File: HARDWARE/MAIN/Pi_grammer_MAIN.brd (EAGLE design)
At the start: 73.7 x 78.7 mm, 51 parts, among them J1 TARGET_copy, Q1 BSS138, Q2 BSS138, Q3 BSS138, Q4 BSS138, U1 AT42QT1010UDFN

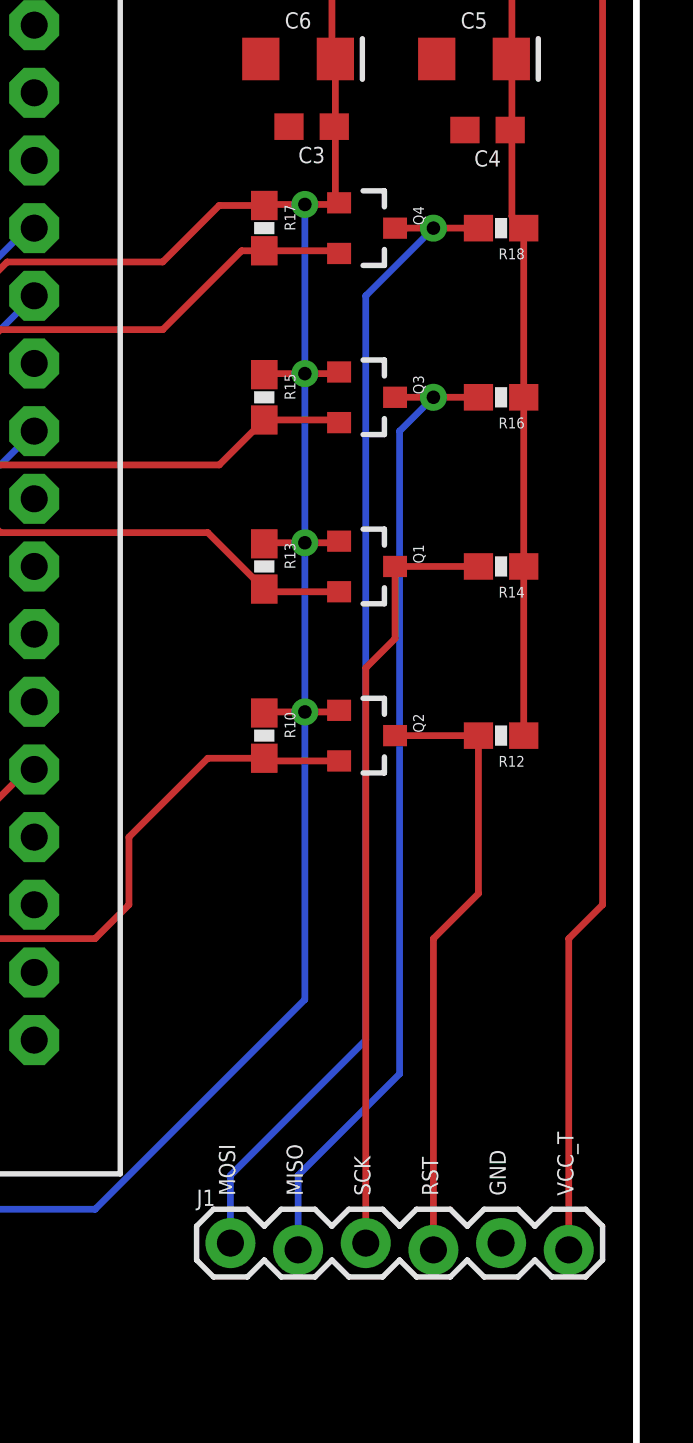
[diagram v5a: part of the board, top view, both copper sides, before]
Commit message: BOM update - library and PROD_ID stuff
No change to design, just did a replace to correct parts in library.

Note, I also had to manually adjust the PROD_ID for the RA header,
because I didn't want to muddy up the device for this part.
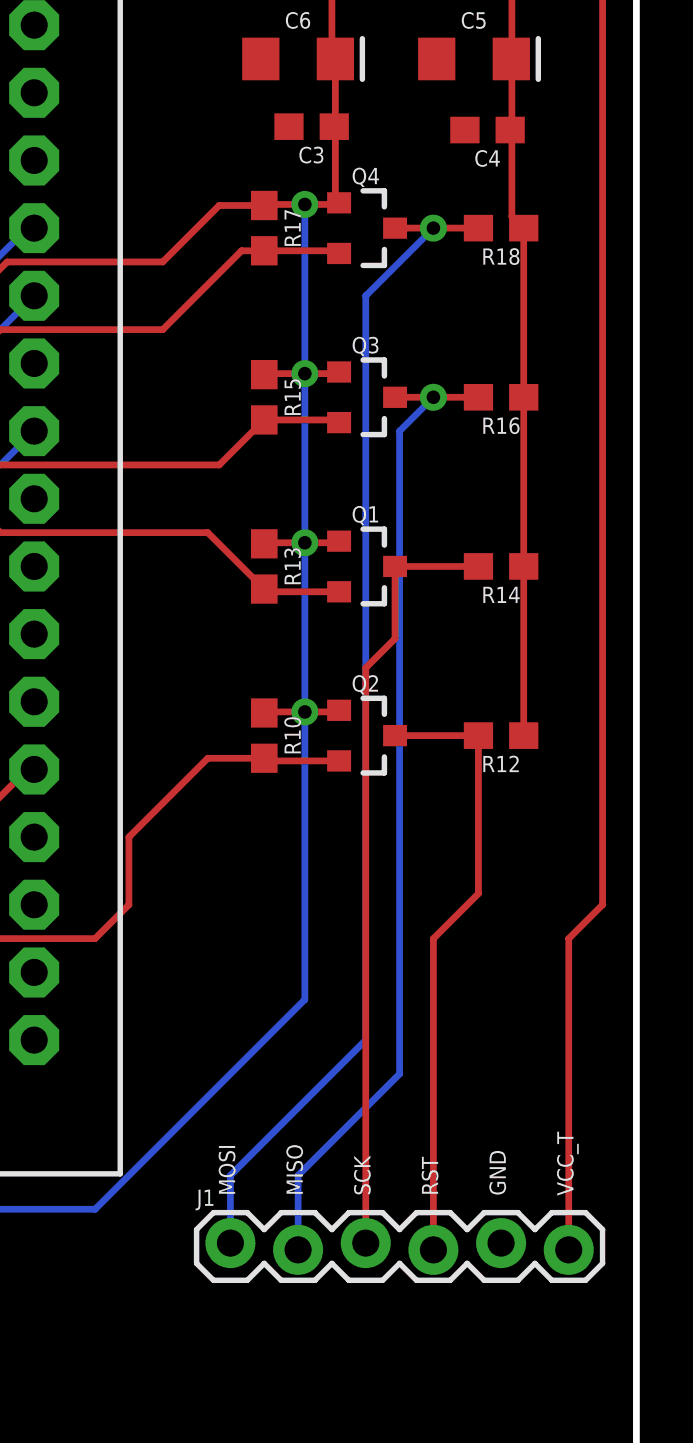
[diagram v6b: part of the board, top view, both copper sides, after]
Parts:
- J1: device SparkFun-Connectors:1X06-SIP_LOCK -> SparkFun-Connectors:1X06_LOCK
- Q1, Q2, Q3, Q4: value BSS138 -> 220mA/50V/3.5Ω; device SparkFun:SOT23-3 -> SparkFun-DiscreteSemi:SOT23-3
- R10, R12, R13, R14, R15, R16, R17, R18: value 10K -> 10k; device SparkFun:0603-RES -> SparkFun-Resistors:0603
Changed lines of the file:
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@@
 <element name="FD1" library="SparkFun-Aesthetics" package="MICRO-FIDUCIAL" value="FIDUCIALUFIDUCIAL" x="2.54" y="76.2"/>
 <element name="FD2" library="SparkFun-Aesthetics" package="MICRO-FIDUCIAL" value="FIDUCIALUFIDUCIAL" x="72.39" y="2.54"/>
-<element name="Q2" library="SparkFun" package="SOT23-3" value="BSS138" x="63.5" y="33.02" rot="R270"/>
-<element name="R10" library="SparkFun" package="0603-RES" value="10K" x="59.69" y="33.02" rot="R270"/>
-<element name="R12" library="SparkFun" package="0603-RES" value="10K" x="68.58" y="33.02" rot="R180"/>
-<element name="Q1" library="SparkFun" package="SOT23-3" value="BSS138" x="63.5" y="39.37" rot="R270"/>
-<element name="R13" library="SparkFun" package="0603-RES" value="10K" x="59.69" y="39.37" rot="R270"/>
-<element name="R14" library="SparkFun" package="0603-RES" value="10K" x="68.58" y="39.37" rot="R180"/>
-<element name="Q3" library="SparkFun" package="SOT23-3" value="BSS138" x="63.5" y="45.72" rot="R270"/>
-<element name="R15" library="SparkFun" package="0603-RES" value="10K" x="59.69" y="45.72" rot="R270"/>
-<element name="R16" library="SparkFun" package="0603-RES" value="10K" x="68.58" y="45.72" rot="R180"/>
-<element name="Q4" library="SparkFun" package="SOT23-3" value="BSS138" x="63.5" y="52.07" rot="R270"/>
-<element name="R17" library="SparkFun" package="0603-RES" value="10K" x="59.69" y="52.07" rot="R270"/>
-<element name="R18" library="SparkFun" package="0603-RES" value="10K" x="68.58" y="52.07" rot="R180"/>
-<element name="J1" library="SparkFun-Connectors" package="1X06-SIP_LOCK" value="TARGET_copy" x="58.42" y="13.97">
-<attribute name="PROD_ID" value="CONN-09698" x="58.42" y="13.97" size="1.778" layer="27" font="vector" ratio="15" display="off"/>
+<element name="Q2" library="SparkFun-DiscreteSemi" package="SOT23-3" value="220mA/50V/3.5Ω" x="63.5" y="33.02" rot="R270">
+<attribute name="PROD_ID" value="TRANS-00830" x="63.5" y="33.02" size="1.778" layer="27" rot="R270" display="off"/>
+<attribute name="VALUE" value="220mA/50V/3.5Ω" x="63.5" y="33.02" size="1.778" layer="27" rot="R270" display="off"/>
+</element>
+<element name="R10" library="SparkFun-Resistors" package="0603" value="10k" x="59.69" y="33.02" rot="R270">
+<attribute name="PROD_ID" value="RES-00824" x="59.69" y="33.02" size="1.778" layer="27" rot="R270" display="off"/>
+<attribute name="VALUE" value="10k" x="59.69" y="33.02" size="1.778" layer="27" rot="R270" display="off"/>
+</element>
+<element name="R12" library="SparkFun-Resistors" package="0603" value="10k" x="68.58" y="33.02" rot="R180">
+<attribute name="PROD_ID" value="RES-00824" x="68.58" y="33.02" size="1.778" layer="27" rot="R180" display="off"/>
+<attribute name="VALUE" value="10k" x="68.58" y="33.02" size="1.778" layer="27" rot="R180" display="off"/>
+</element>
+<element name="Q1" library="SparkFun-DiscreteSemi" package="SOT23-3" value="220mA/50V/3.5Ω" x="63.5" y="39.37" rot="R270">
+<attribute name="PROD_ID" value="TRANS-00830" x="63.5" y="39.37" size="1.778" layer="27" rot="R270" display="off"/>
+<attribute name="VALUE" value="220mA/50V/3.5Ω" x="63.5" y="39.37" size="1.778" layer="27" rot="R270" display="off"/>
+</element>
+<element name="R13" library="SparkFun-Resistors" package="0603" value="10k" x="59.69" y="39.37" rot="R270">
+<attribute name="PROD_ID" value="RES-00824" x="59.69" y="39.37" size="1.778" layer="27" rot="R270" display="off"/>
+<attribute name="VALUE" value="10k" x="59.69" y="39.37" size="1.778" layer="27" rot="R270" display="off"/>
+</element>
+<element name="R14" library="SparkFun-Resistors" package="0603" value="10k" x="68.58" y="39.37" rot="R180">
+<attribute name="PROD_ID" value="RES-00824" x="68.58" y="39.37" size="1.778" layer="27" rot="R180" display="off"/>
+<attribute name="VALUE" value="10k" x="68.58" y="39.37" size="1.778" layer="27" rot="R180" display="off"/>
+</element>
+<element name="Q3" library="SparkFun-DiscreteSemi" package="SOT23-3" value="220mA/50V/3.5Ω" x="63.5" y="45.72" rot="R270">
+<attribute name="PROD_ID" value="TRANS-00830" x="63.5" y="45.72" size="1.778" layer="27" rot="R270" display="off"/>
+<attribute name="VALUE" value="220mA/50V/3.5Ω" x="63.5" y="45.72" size="1.778" layer="27" rot="R270" display="off"/>
+</element>
+<element name="R15" library="SparkFun-Resistors" package="0603" value="10k" x="59.69" y="45.72" rot="R270">
+<attribute name="PROD_ID" value="RES-00824" x="59.69" y="45.72" size="1.778" layer="27" rot="R270" display="off"/>
+<attribute name="VALUE" value="10k" x="59.69" y="45.72" size="1.778" layer="27" rot="R270" display="off"/>
+</element>
+<element name="R16" library="SparkFun-Resistors" package="0603" value="10k" x="68.58" y="45.72" rot="R180">
+<attribute name="PROD_ID" value="RES-00824" x="68.58" y="45.72" size="1.778" layer="27" rot="R180" display="off"/>
+<attribute name="VALUE" value="10k" x="68.58" y="45.72" size="1.778" layer="27" rot="R180" display="off"/>
+</element>
+<element name="Q4" library="SparkFun-DiscreteSemi" package="SOT23-3" value="220mA/50V/3.5Ω" x="63.5" y="52.07" rot="R270">
+<attribute name="PROD_ID" value="TRANS-00830" x="63.5" y="52.07" size="1.778" layer="27" rot="R270" display="off"/>
+<attribute name="VALUE" value="220mA/50V/3.5Ω" x="63.5" y="52.07" size="1.778" layer="27" rot="R270" display="off"/>
+</element>
+<element name="R17" library="SparkFun-Resistors" package="0603" value="10k" x="59.69" y="52.07" rot="R270">
+<attribute name="PROD_ID" value="RES-00824" x="59.69" y="52.07" size="1.778" layer="27" rot="R270" display="off"/>
+<attribute name="VALUE" value="10k" x="59.69" y="52.07" size="1.778" layer="27" rot="R270" display="off"/>
+</element>
+<element name="R18" library="SparkFun-Resistors" package="0603" value="10k" x="68.58" y="52.07" rot="R180">
+<attribute name="PROD_ID" value="RES-00824" x="68.58" y="52.07" size="1.778" layer="27" rot="R180" display="off"/>
+<attribute name="VALUE" value="10k" x="68.58" y="52.07" size="1.778" layer="27" rot="R180" display="off"/>
+</element>
+<element name="J1" library="SparkFun-Connectors" package="1X06_LOCK" value="TARGET_copy" x="58.42" y="13.97">
+<attribute name="PROD_ID" value="CONN-10140" x="58.42" y="13.97" size="1.778" layer="27" font="vector" ratio="15" display="off"/>
 </element>
 <element name="JP5" library="SparkFun-Jumpers" package="SMT-JUMPER_2_NO_SILK" value="" x="68.58" y="69.85" rot="R180"/>

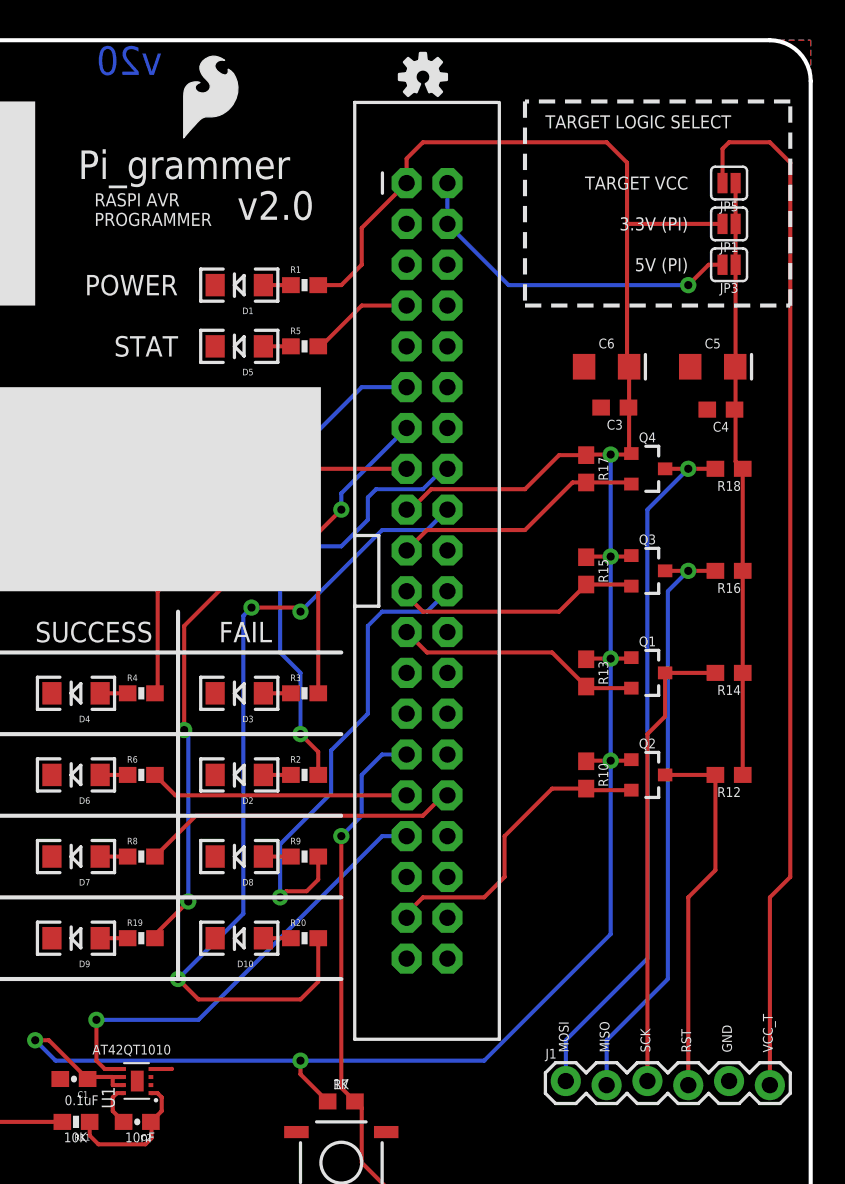
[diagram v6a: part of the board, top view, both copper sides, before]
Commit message: pi_grammer v21
Added in isolation switch
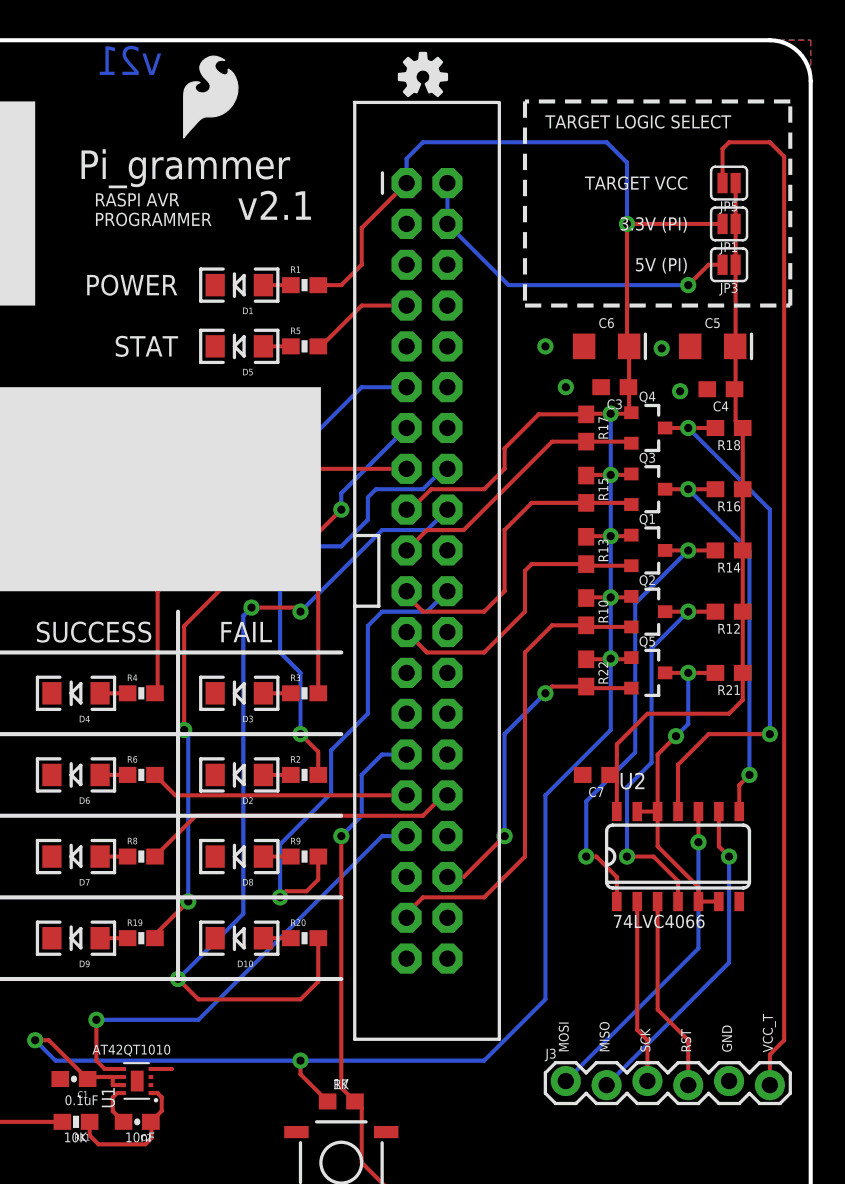
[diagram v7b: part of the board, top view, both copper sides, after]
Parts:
- added C7: 0.1uF, SparkFun-Capacitors:0603
- added Q5: 220mA/50V/3.5Ω, SparkFun-DiscreteSemi:SOT23-3
- added R21, R22: 10k, SparkFun-Resistors:0603
- added U2: 74LVC4066, Testing:SO14
- moved Q2 10.2 mm to (63.5, 43.2)
- moved R10 10.2 mm to (59.7, 43.2)
- moved R12 10.2 mm to (68.6, 43.2)
- moved Q1 7.62 mm to (63.5, 47.0)
- moved R13 7.62 mm to (59.7, 47.0)
- moved R14 7.62 mm to (68.6, 47.0)
- moved Q3 5.08 mm to (63.5, 50.8)
- moved R15 5.08 mm to (59.7, 50.8)
- moved R16 5.08 mm to (68.6, 50.8)
- moved Q4 2.54 mm to (63.5, 54.6)
- moved R17 2.54 mm to (59.7, 54.6)
- moved R18 2.54 mm to (68.6, 54.6)
- moved C4 1.27 mm to (68.1, 57.0)
- moved C3 1.27 mm to (61.5, 57.1)
- moved C5 1.27 mm to (67.6, 59.7)
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- renumbered J1 to J3
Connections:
- removed net N$9: C4.1, C5.+, JP1.1, JP3.1, JP5.1, R12.1, R14.1, R16.1, R18.1
- new net BRD_MISO: J3.2, U2.9
- new net BRD_MOSI: J3.1, U2.10
- new net BRD_RST: J3.4, U2.3
- new net BRD_SCK: J3.3, U2.2
- new net PGM_CTRL: JP2.36, Q5.2, R22.2
- new net PGM_CTRL_T: Q5.3, R21.2, U2.12, U2.13, U2.5, U2.6
- new net VCC_T_SELECTED: C4.1, C5.+, C7.1, JP1.1, JP3.1, JP5.1, R12.1, R14.1, R16.1, R18.1, R21.1, U2.14
- net 3.3V: now also Q5.1, R22.1
- net GND: now also C7.2, U2.7
- net MISO_T: now also U2.8; no longer J3.2
- net MOSI_T: now also U2.11; no longer J3.1
- net RST_T: now also U2.4; no longer J3.4
- net SCK_T: now also U2.1; no longer J3.3
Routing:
- net VCC_T_SELECTED: track 0.00 -> 46.3 mm
- net N$9: track 37.2 -> 0.00 mm
- net PGM_CTRL_T: track 0.00 -> 21.7 mm, vias 0 -> 2
- net BRD_MISO: track 0.00 -> 20.4 mm, vias 0 -> 1
- net BRD_MOSI: track 0.00 -> 20.2 mm, vias 0 -> 1
- net PGM_CTRL: track 0.00 -> 20.1 mm, vias 0 -> 2
- net BRD_RST: track 0.00 -> 12.2 mm
- net MISO_T: track 37.2 -> 25.0 mm, vias 1 -> 2
- net BRD_SCK: track 0.00 -> 11.4 mm
- net MOSI_T: track 44.4 -> 33.7 mm, vias 1 -> 2
- net RST: track 19.0 -> 29.2 mm
- net 3.3V: track 154.4 -> 159.1 mm, vias 6 -> 8
- net MISO: track 15.4 -> 19.7 mm
- net SCK: track 15.4 -> 18.3 mm
- net RST_T: track 23.1 -> 25.0 mm, vias 0 -> 2
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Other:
- board text added: "v2.1"
- board text added: "v21"
- board text removed: "v2.0"
- board text removed: "v20"

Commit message: Swapped out package to paste-closed jumper for TARGET VCC
This needed a default target logic select. It is now closed (selected) via paste on the "TARGET VCC" option.
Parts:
- JP5: value (none) -> JUMPER-SMT_2_NC_PASTE_SILK; device SparkFun-Jumpers:SMT-JUMPER_2_NO_SILK -> SparkFun-Jumpers:SMT-JUMPER_2_NC_PASTE_SILK
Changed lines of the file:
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@@
 <?xml version="1.0" encoding="utf-8"?>
 <!DOCTYPE eagle SYSTEM "eagle.dtd">
-<eagle version="6.5.0">
+<eagle version="7.6.0">
 <drawing>
 <settings>
@@
 <layer number="29" name="tStop" color="7" fill="3" visible="no" active="yes"/>
 <layer number="30" name="bStop" color="7" fill="6" visible="no" active="yes"/>
-<layer number="31" name="tCream" color="7" fill="4" visible="no" active="yes"/>
+<layer number="31" name="tCream" color="7" fill="4" visible="yes" active="yes"/>
 <layer number="32" name="bCream" color="7" fill="5" visible="no" active="yes"/>
 <layer number="33" name="tFinish" color="6" fill="3" visible="no" active="yes"/>
@@
 <layer number="47" name="Measures" color="7" fill="1" visible="no" active="yes"/>
 <layer number="48" name="Document" color="7" fill="1" visible="no" active="yes"/>
-<layer number="49" name="Reference" color="13" fill="1" visible="yes" active="yes"/>
+<layer number="49" name="Reference" color="13" fill="1" visible="no" active="yes"/>
 <layer number="50" name="dxf" color="7" fill="1" visible="no" active="yes"/>
 <layer number="51" name="tDocu" color="6" fill="1" visible="yes" active="yes"/>
@@
 <pass name="Default">
 <param name="RoutingGrid" value="50mil"/>
+<param name="AutoGrid" value="1"/>
+<param name="Efforts" value="0"/>
+<param name="TopRouterVariant" value="1"/>
 <param name="tpViaShape" value="round"/>
 <param name="PrefDir.1" value="|"/>
@@
 <attribute name="VALUE" value="10k" x="68.58" y="54.61" size="1.778" layer="27" rot="R180" display="off"/>
 </element>
-<element name="JP5" library="SparkFun-Jumpers" package="SMT-JUMPER_2_NO_SILK" value="" x="68.58" y="69.85" rot="R180"/>
+<element name="JP5" library="SparkFun-Jumpers" package="SMT-JUMPER_2_NC_PASTE_SILK" value="JUMPER-SMT_2_NC_PASTE_SILK" x="68.58" y="69.85" rot="R180"/>
 <element name="JP1" library="SparkFun-Jumpers" package="SMT-JUMPER_2_NO_SILK" value="" x="68.58" y="67.31" rot="R180"/>
 <element name="JP3" library="SparkFun-Jumpers" package="SMT-JUMPER_2_NO_SILK" value="" x="68.58" y="64.77" rot="R180"/>
